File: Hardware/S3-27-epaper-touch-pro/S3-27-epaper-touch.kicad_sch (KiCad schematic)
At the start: 61 parts, among them J1 AFC24-S24FIC-00, J2 USB_C_Programming, J3 Conn_01x06, J4 Conn_01x06_Female, J5 Groove sensor, J6 Conn_01x06, Q1 Si1308, Q2 BC817, Q3 BC817, U1 ESP32-S3-WROOM-1-N8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

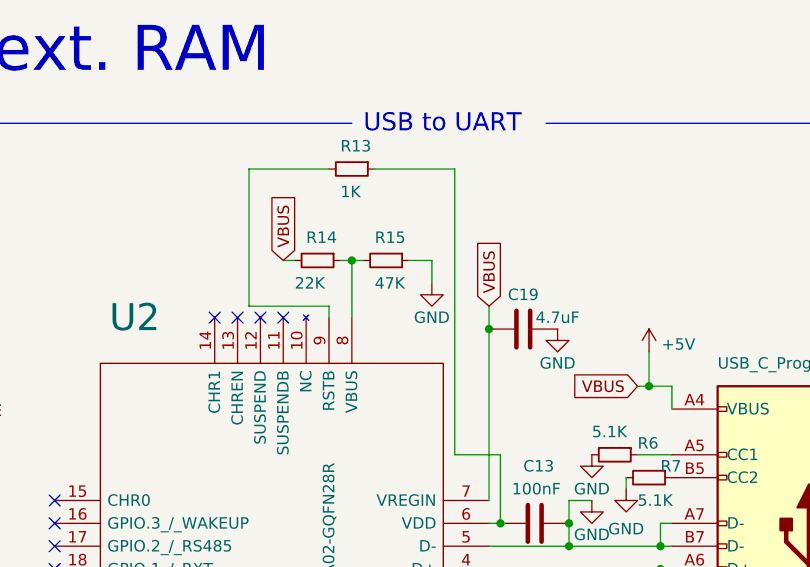
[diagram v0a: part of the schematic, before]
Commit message: Update R15 thx. @Uspizig
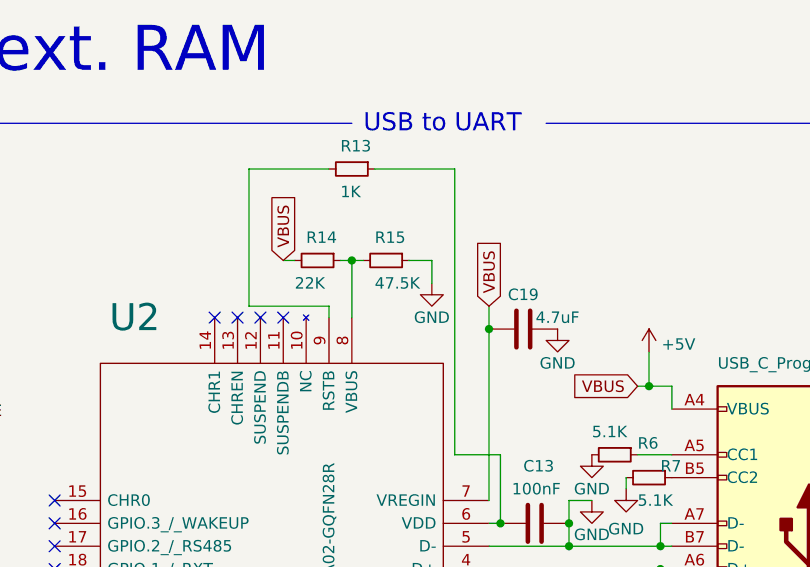
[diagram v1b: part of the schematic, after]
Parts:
- R15: value 47K -> 47.5K; footprint Resistor_SMD:R_0402_1005Metric -> Resistor_SMD:R_0603_1608Metric; LCSC C137974 -> C103667
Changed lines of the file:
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@@
       (effects (font (size 1.27 1.27)) (justify left))
     )
-    (property "Value" "47K" (id 1) (at 312.42 44.45 90)
+    (property "Value" "47.5K" (id 1) (at 312.42 44.45 90)
       (effects (font (size 1.27 1.27)) (justify left))
     )
-    (property "Footprint" "Resistor_SMD:R_0402_1005Metric" (id 2) (at 313.69 41.91 0)
-      (effects (font (size 1.27 1.27)) hide)
-    )
-    (property "Datasheet" "https://jlcpcb.com/partdetail/Yageo-RC0402FR0747K5L/C137974" (id 3) (at 313.69 41.91 0)
-      (effects (font (size 1.27 1.27)) hide)
-    )
-    (property "LCSC" "C137974" (id 4) (at 313.69 41.91 90)
+    (property "Footprint" "Resistor_SMD:R_0603_1608Metric" (id 2) (at 313.69 41.91 0)
+      (effects (font (size 1.27 1.27)) hide)
+    )
+    (property "Datasheet" "https://jlcpcb.com/partdetail/Ralec-RTT034752FTP/C103667" (id 3) (at 313.69 41.91 0)
+      (effects (font (size 1.27 1.27)) hide)
+    )
+    (property "LCSC" "C103667" (id 4) (at 313.69 41.91 90)
       (effects (font (size 1.27 1.27)) hide)
     )
@@
     )
     (path "/f03960ef-9e49-45d2-a9fd-2f2de73439b2"
-      (reference "R15") (unit 1) (value "47K") (footprint "Resistor_SMD:R_0402_1005Metric")
+      (reference "R15") (unit 1) (value "47.5K") (footprint "Resistor_SMD:R_0603_1608Metric")
     )
     (path "/21439738-76b8-4267-91fd-2ea304ae429f"

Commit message: Error detected by @ispizig. Thanks!
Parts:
- U1: value ESP32-S3-WROOM-1-N8 -> ESP32-S3
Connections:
- net GND: no longer J2.A7 (D-), J2.B7 (D-), U2.5 (D-)
- new net: J2.A7 (D-), J2.B7 (D-), U2.5 (D-)
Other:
- note added: "WROOM-1-N8"
- moved on the sheet: C13, R6, R7
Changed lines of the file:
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@@
   (junction (at 109.22 125.73) (diameter 0) (color 0 0 0 0)
   )
-  (junction (at 326.39 71.12) (diameter 0) (color 0 0 0 0)
+  (junction (at 326.39 68.58) (diameter 0) (color 0 0 0 0)
   )
   (junction (at 201.93 54.61) (diameter 0) (color 0 0 0 0)
   )
-  (junction (at 334.01 71.12) (diameter 0) (color 0 0 0 0)
-  )
   (junction (at 60.96 129.54) (diameter 0) (color 0 0 0 0)
   )
@@
   (junction (at 99.06 74.93) (diameter 0) (color 0 0 0 0)
   )
-  (junction (at 334.01 73.66) (diameter 0) (color 0 0 0 0)
-  )
   (junction (at 68.58 72.39) (diameter 0) (color 0 0 0 0)
   )
@@
     (stroke (width 0) (type default) (color 0 0 0 0))
   )
-  (wire (pts (xy 334.01 71.12) (xy 334.01 73.66))
-    (stroke (width 0) (type default) (color 0 0 0 0))
-  )
   (wire (pts (xy 153.67 53.34) (xy 153.67 57.15))
     (stroke (width 0) (type default) (color 0 0 0 0))
@@
     (stroke (width 0) (type default) (color 0 0 0 0))
   )
-  (wire (pts (xy 326.39 63.5) (xy 326.39 71.12))
+  (wire (pts (xy 326.39 63.5) (xy 326.39 68.58))
     (stroke (width 0) (type default) (color 0 0 0 0))
   )
@@
     (stroke (width 0) (type default) (color 0 0 0 0))
   )
-  (wire (pts (xy 336.55 68.58) (xy 334.01 68.58))
-    (stroke (width 0) (type default) (color 0 0 0 0))
-  )
   (wire (pts (xy 63.5 172.72) (xy 63.5 170.18))
     (stroke (width 0) (type default) (color 0 0 0 0))
@@
     (stroke (width 0) (type default) (color 0 0 0 0))
   )
-  (wire (pts (xy 325.12 73.66) (xy 334.01 73.66))
+  (wire (pts (xy 325.12 73.66) (xy 344.17 73.66))
     (stroke (width 0) (type default) (color 0 0 0 0))
   )
@@
     (stroke (width 0) (type default) (color 0 0 0 0))
   )
-  (wire (pts (xy 334.01 68.58) (xy 334.01 71.12))
-    (stroke (width 0) (type default) (color 0 0 0 0))
-  )
   (polyline (pts (xy 326.39 161.29) (xy 326.39 175.26))
     (stroke (width 0) (type default) (color 0 0 0 0))
@@
     (stroke (width 0) (type default) (color 0 0 0 0))
   )
-  (wire (pts (xy 340.36 67.31) (xy 340.36 66.04))
-    (stroke (width 0) (type default) (color 0 0 0 0))
-  )
   (wire (pts (xy 87.63 176.53) (xy 87.63 179.07))
     (stroke (width 0) (type default) (color 0 0 0 0))
@@
     (stroke (width 0) (type default) (color 0 0 0 0))
   )
+  (wire (pts (xy 326.39 68.58) (xy 326.39 71.12))
+    (stroke (width 0) (type default) (color 0 0 0 0))
+  )
   (wire (pts (xy 160.02 90.17) (xy 161.29 90.17))
     (stroke (width 0) (type default) (color 0 0 0 0))
@@
     (stroke (width 0) (type default) (color 0 0 0 0))
   )
-  (wire (pts (xy 334.01 73.66) (xy 344.17 73.66))
-    (stroke (width 0) (type default) (color 0 0 0 0))
-  )
   (wire (pts (xy 167.64 185.42) (xy 168.91 185.42))
     (stroke (width 0) (type default) (color 0 0 0 0))
@@
     (stroke (width 0) (type default) (color 0 0 0 0))
   )
-  (wire (pts (xy 204.47 62.23) (xy 201.93 62.23))
+  (wire (pts (xy 345.44 67.31) (xy 345.44 66.04))
     (stroke (width 0) (type default) (color 0 0 0 0))
   )
-  (wire (pts (xy 341.63 63.5) (xy 345.44 63.5))
+  (wire (pts (xy 204.47 62.23) (xy 201.93 62.23))
     (stroke (width 0) (type default) (color 0 0 0 0))
   )
@@
     (stroke (width 0) (type default) (color 0 0 0 0))
   )
+  (wire (pts (xy 340.36 63.5) (xy 337.82 63.5))
+    (stroke (width 0) (type default) (color 0 0 0 0))
+  )
   (wire (pts (xy 161.29 54.61) (xy 158.75 54.61))
     (stroke (width 0) (type default) (color 0 0 0 0))
@@
     (effects (font (size 1.27 1.27)) (justify left bottom))
   )
+  (text "WROOM-1-N8" (at 181.61 49.53 0)
+    (effects (font (size 1.524 1.524)) (justify left bottom))
+  )
   (text "VSS" (at 60.96 110.49 0)
     (effects (font (size 1.27 1.27)) (justify left bottom))
@@
     (pin "1")
   )
-  (symbol (lib_id "Device:R_Small") (at 339.09 63.5 270) (unit 1)
+  (symbol (lib_id "Device:R_Small") (at 342.9 63.5 270) (unit 1)
     (in_bom yes) (on_board yes)
-    (property "Reference" "R6" (id 0) (at 341.63 62.23 90)
+    (property "Reference" "R6" (id 0) (at 341.63 63.5 90)
       (effects (font (size 1.27 1.27)) (justify left))
     )
-    (property "Value" "5.1K" (id 1) (at 336.55 60.96 90)
+    (property "Value" "5.1K" (id 1) (at 340.36 60.96 90)
       (effects (font (size 1.27 1.27)) (justify left))
     )
-    (property "Footprint" "Resistor_SMD:R_0603_1608Metric" (id 2) (at 339.09 63.5 0)
+    (property "Footprint" "Resistor_SMD:R_0603_1608Metric" (id 2) (at 342.9 63.5 0)
       (effects (font (size 1.27 1.27)) hide)
     )
-    (property "Datasheet" "https://datasheet.lcsc.com/lcsc/2206010116_UNI-ROYAL-Uniroyal-Elec-0603WAF5101T5E_C23186.pdf" (id 3) (at 339.09 63.5 0)
+    (property "Datasheet" "https://datasheet.lcsc.com/lcsc/2206010116_UNI-ROYAL-Uniroyal-Elec-0603WAF5101T5E_C23186.pdf" (id 3) (at 342.9 63.5 0)
       (effects (font (size 1.27 1.27)) hide)
     )
-    (property "LCSC" "C23186" (id 4) (at 339.09 63.5 90)
+    (property "LCSC" "C23186" (id 4) (at 342.9 63.5 90)
       (effects (font (size 1.27 1.27)) hide)
     )
@@
     (pin "2")
   )
-  (symbol (lib_id "power:GND") (at 336.55 68.58 0) (unit 1)
+  (symbol (lib_id "power:GND") (at 334.01 68.58 0) (unit 1)
     (in_bom yes) (on_board yes)
-    (property "Reference" "#PWR020" (id 0) (at 336.55 74.93 0)
+    (property "Reference" "#PWR020" (id 0) (at 334.01 74.93 0)
       (effects (font (size 1.27 1.27)) hide)
     )
-    (property "Value" "GND" (id 1) (at 336.55 72.39 0))
-    (property "Footprint" "" (id 2) (at 336.55 68.58 0)
+    (property "Value" "GND" (id 1) (at 334.01 72.39 0))
+    (property "Footprint" "" (id 2) (at 334.01 68.58 0)
       (effects (font (size 1.27 1.27)) hide)
     )
-    (property "Datasheet" "" (id 3) (at 336.55 68.58 0)
+    (property "Datasheet" "" (id 3) (at 334.01 68.58 0)
       (effects (font (size 1.27 1.27)) hide)
     )
     (pin "1")
   )
-  (symbol (lib_id "Device:R_Small") (at 342.9 66.04 270) (unit 1)
+  (symbol (lib_id "Device:R_Small") (at 342.9 67.31 270) (unit 1)
     (in_bom yes) (on_board yes)
-    (property "Reference" "R7" (id 0) (at 344.17 64.77 90)
+    (property "Reference" "R7" (id 0) (at 341.63 67.31 90)
       (effects (font (size 1.27 1.27)) (justify left))
     )
-    (property "Value" "5.1K" (id 1) (at 341.63 68.58 90)
+    (property "Value" "5.1K" (id 1) (at 341.63 69.85 90)
       (effects (font (size 1.27 1.27)) (justify left))
     )
-    (property "Footprint" "Resistor_SMD:R_0603_1608Metric" (id 2) (at 342.9 66.04 0)
+    (property "Footprint" "Resistor_SMD:R_0603_1608Metric" (id 2) (at 342.9 67.31 0)
       (effects (font (size 1.27 1.27)) hide)
     )
-    (property "Datasheet" "https://datasheet.lcsc.com/lcsc/2206010116_UNI-ROYAL-Uniroyal-Elec-0603WAF5101T5E_C23186.pdf" (id 3) (at 342.9 66.04 0)
+    (property "Datasheet" "https://datasheet.lcsc.com/lcsc/2206010116_UNI-ROYAL-Uniroyal-Elec-0603WAF5101T5E_C23186.pdf" (id 3) (at 342.9 67.31 0)
       (effects (font (size 1.27 1.27)) hide)
     )
-    (property "LCSC" "C23186" (id 4) (at 342.9 66.04 90)
+    (property "LCSC" "C23186" (id 4) (at 342.9 67.31 90)
       (effects (font (size 1.27 1.27)) hide)
     )
@@
     )
   )
-  (symbol (lib_id "power:GND") (at 336.55 63.5 0) (unit 1)
+  (symbol (lib_id "power:GND") (at 337.82 63.5 0) (unit 1)
     (in_bom yes) (on_board yes)
-    (property "Reference" "#PWR03" (id 0) (at 336.55 69.85 0)
+    (property "Reference" "#PWR03" (id 0) (at 337.82 69.85 0)
       (effects (font (size 1.27 1.27)) hide)
     )
-    (property "Value" "GND" (id 1) (at 336.55 67.31 0))
-    (property "Footprint" "" (id 2) (at 336.55 63.5 0)
+    (property "Value" "GND" (id 1) (at 337.82 67.31 0))
+    (property "Footprint" "" (id 2) (at 337.82 63.5 0)
       (effects (font (size 1.27 1.27)) hide)
     )
-    (property "Datasheet" "" (id 3) (at 336.55 63.5 0)
+    (property "Datasheet" "" (id 3) (at 337.82 63.5 0)
       (effects (font (size 1.27 1.27)) hide)
     )
@@
   )
   (symbol (lib_id "ESP332S3:ESP32-S3-WROOM-1-N8") (at 161.29 54.61 0) (unit 1)
-    (in_bom yes) (on_board yes) (fields_autoplaced)
+    (in_bom yes) (on_board yes)
     (property "Reference" "U1" (id 0) (at 181.61 45.3824 0)
       (effects (font (size 1.524 1.524)))
     )
-    (property "Value" "ESP32-S3-WROOM-1-N8" (id 1) (at 181.61 48.3758 0)
+    (property "Value" "ESP32-S3" (id 1) (at 175.26 48.26 0)
       (effects (font (size 1.524 1.524)))
     )
@@
     (pin "1")
   )
-  (symbol (lib_id "Device:C") (at 330.2 71.12 90) (unit 1)
+  (symbol (lib_id "Device:C") (at 330.2 68.58 90) (unit 1)
     (in_bom yes) (on_board yes)
-    (property "Reference" "C13" (id 0) (at 328.93 64.77 90)
+    (property "Reference" "C13" (id 0) (at 328.93 62.23 90)
       (effects (font (size 1.27 1.27)) (justify right))
     )
-    (property "Value" "100nF" (id 1) (at 327.66 67.31 90)
+    (property "Value" "100nF" (id 1) (at 327.66 64.77 90)
       (effects (font (size 1.27 1.27)) (justify right))
     )
-    (property "Footprint" "Capacitor_SMD:C_0805_2012Metric" (id 2) (at 334.01 70.1548 0)
+    (property "Footprint" "Capacitor_SMD:C_0805_2012Metric" (id 2) (at 334.01 67.6148 0)
       (effects (font (size 1.27 1.27)) hide)
     )
-    (property "Datasheet" "~" (id 3) (at 330.2 71.12 0)
+    (property "Datasheet" "~" (id 3) (at 330.2 68.58 0)
       (effects (font (size 1.27 1.27)) hide)
     )
-    (property "LCSC" "C28233" (id 4) (at 330.2 71.12 0)
+    (property "LCSC" "C28233" (id 4) (at 330.2 68.58 0)
       (effects (font (size 1.27 1.27)) hide)
     )
@@
     )
     (path "/a7875a93-ab9c-4fbd-a887-6c4f7f50e845"
-      (reference "U1") (unit 1) (value "ESP32-S3-WROOM-1-N8") (footprint "footprint:ESP32-S3-WROOM-1-N8")
+      (reference "U1") (unit 1) (value "ESP32-S3") (footprint "footprint:ESP32-S3-WROOM-1-N8")
     )
     (path "/828b5c01-bbdd-4cc3-a771-72e50c03bfc6"

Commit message: S3 update to review: No more C 220uF RTC backup use CR1220
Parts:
- removed C17, C18: 220uF, Capacitor_Tantalum_SMD:CP_EIA-3528-21_Kemet-B, symbol Device:C_Polarized
- removed D4: 1N5819WS, Diode_SMD:D_SOD-323, symbol Diode:MBR0530
- removed TP2: TX, TestPoint:TestPoint_Pad_D1.5mm, symbol Connector:TestPoint
- removed TP6: RX, TestPoint:TestPoint_Pad_D1.5mm, symbol Connector:TestPoint
- added BT1: CR1220, footprint:CR12202ZX, symbol Device:Battery_Cell
- J5: footprint footprint:MOLEX-I2C-532530470 -> footprint:MOLEX-I2C-Groove
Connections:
- net GND: now also BT1.2 (-)
- net at U4.6 (VBAT): now also BT1.1 (+)

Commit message: Update S3 heading to 1.1 release
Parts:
- J5: value Groove sensor -> GROVE
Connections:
- net +3V3: now also J5.2; no longer J5.3
- net GND: now also J5.1; no longer J5.4
- net TOUCH_SCL: now also J5.4; no longer J5.1
- net TOUCH_SDA: now also J5.3; no longer J5.2
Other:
- note added: "Grove I2C connector"
- note removed: "Groove I2C connector"
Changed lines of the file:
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@@
     (effects (font (size 1.27 1.27)) (justify left bottom))
   )
-  (text "Groove I2C connector" (at 167.64 218.44 0)
+  (text "Grove I2C connector" (at 167.64 218.44 0)
     (effects (font (size 2 2)) (justify left bottom))
   )
@@
     (pin "1")
     (pin "2")
-  )
-  (symbol (lib_id "MOLEX-I2C-532530470:532530470") (at 186.69 233.68 0) (mirror y) (unit 1)
-    (in_bom yes) (on_board yes)
-    (property "Reference" "J5" (id 0) (at 177.8 226.9924 0)
-      (effects (font (size 1.524 1.524)))
-    )
-    (property "Value" "Groove sensor" (id 1) (at 180.34 229.87 0)
-      (effects (font (size 1.524 1.524)))
-    )
-    (property "Footprint" "footprint:MOLEX-I2C-Groove" (id 2) (at 176.53 240.284 0)
-      (effects (font (size 1.524 1.524)) hide)
-    )
-    (property "Datasheet" "" (id 3) (at 186.69 233.68 0)
-      (effects (font (size 1.524 1.524)))
-    )
-    (pin "1")
-    (pin "2")
-    (pin "3")
-    (pin "4")
   )
   (symbol (lib_id "Connector:TestPoint") (at 67.31 137.16 0) (unit 1)
@@
       (effects (font (size 1.27 1.27)) hide)
     )
-    (property "Datasheet" "~" (id 3) (at 70.104 175.26 90)
+    (property "Datasheet" "C969906" (id 3) (at 70.104 175.26 90)
       (effects (font (size 1.27 1.27)) hide)
     )
@@
     (pin "2")
   )
+  (symbol (lib_id "MOLEX-I2C-532530470:532530470") (at 186.69 241.3 180) (unit 1)
+    (in_bom yes) (on_board yes)
+    (property "Reference" "J5" (id 0) (at 177.8 247.9876 0)
+      (effects (font (size 1.524 1.524)))
+    )
+    (property "Value" "GROVE" (id 1) (at 180.34 245.11 0)
+      (effects (font (size 1.524 1.524)))
+    )
+    (property "Footprint" "footprint:MOLEX-I2C-Groove" (id 2) (at 176.53 234.696 0)
+      (effects (font (size 1.524 1.524)) hide)
+    )
+    (property "Datasheet" "" (id 3) (at 186.69 241.3 0)
+      (effects (font (size 1.524 1.524)))
+    )
+    (pin "1")
+    (pin "2")
+    (pin "3")
+    (pin "4")
+  )
   (symbol (lib_id "Device:R_Small") (at 143.51 57.15 0) (unit 1)
     (in_bom yes) (on_board yes)
@@
       (reference "J4") (unit 1) (value "Conn_01x06_Female") (footprint "footprint:FH34SRJ-6S-0.5SH50-Hirose")
     )
-    (path "/20915515-cc0c-4430-855a-6af288463492"
-      (reference "J5") (unit 1) (value "Groove sensor") (footprint "footprint:MOLEX-I2C-Groove")
+    (path "/bd571d13-85b1-404e-8590-e8a4d4fa4df4"
+      (reference "J5") (unit 1) (value "GROVE") (footprint "footprint:MOLEX-I2C-Groove")
     )
     (path "/4d28500a-f271-4acd-b4ef-337b67a0b6ea"
